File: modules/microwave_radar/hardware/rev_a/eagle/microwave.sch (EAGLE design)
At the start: 55 parts, among them J1 MODULE_GENERIC, J2 TC2030-JLINK-L, U1 SAM4LC8AA, U2 TLV62130, U3 MSGEQ7

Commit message: First try of routing. Fill in several attributes
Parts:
- C10, C11, C12, C14, C9: DIGIKEY (none) -> 490-10777-1-ND
- C13: DIGIKEY (none) -> 490-13252-1-ND
- C6, C8: DIGIKEY (none) -> 490-8230-1-ND
- L1: DIGIKEY (none) -> 490-5216-1-ND
- R10, R9: DIGIKEY (none) -> 1276-3432-1-ND
- R11: DIGIKEY (none) -> 1276-3431-1-ND
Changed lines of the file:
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@@
 </part>
 <part name="X1" library="crystals" deviceset="FH1600015" device=""/>
-<part name="C6" library="passives" deviceset="CAPACITOR" device="0402_CAP" value="8pF"/>
-<part name="C8" library="passives" deviceset="CAPACITOR" device="0402_CAP" value="8pF"/>
+<part name="C6" library="passives" deviceset="CAPACITOR" device="0402_CAP" value="8pF">
+<attribute name="DIGIKEY" value="490-8230-1-ND"/>
+</part>
+<part name="C8" library="passives" deviceset="CAPACITOR" device="0402_CAP" value="8pF">
+<attribute name="DIGIKEY" value="490-8230-1-ND"/>
+</part>
 <part name="SUPPLY5" library="supply1" deviceset="GND" device=""/>
 <part name="SUPPLY6" library="supply1" deviceset="GND" device=""/>
 <part name="J2" library="connector" deviceset="TC2030-JLINK" device="-L"/>
 <part name="SUPPLY7" library="supply1" deviceset="GND" device=""/>
-<part name="R9" library="passives" deviceset="RESISTOR" device="0402_RES" value="100k"/>
-<part name="R10" library="passives" deviceset="RESISTOR" device="0402_RES" value="100k"/>
-<part name="C9" library="passives" deviceset="CAPACITOR" device="0402_CAP" value="100n"/>
-<part name="C10" library="passives" deviceset="CAPACITOR" device="0402_CAP" value="100n"/>
-<part name="C11" library="passives" deviceset="CAPACITOR" device="0402_CAP" value="100n"/>
-<part name="L1" library="passives" deviceset="FERRITE_BEAD" device="0402" value="1.5k"/>
-<part name="C12" library="passives" deviceset="CAPACITOR" device="0402_CAP" value="100n"/>
+<part name="R9" library="passives" deviceset="RESISTOR" device="0402_RES" value="100k">
+<attribute name="DIGIKEY" value="1276-3432-1-ND"/>
+</part>
+<part name="R10" library="passives" deviceset="RESISTOR" device="0402_RES" value="100k">
+<attribute name="DIGIKEY" value="1276-3432-1-ND"/>
+</part>
+<part name="C9" library="passives" deviceset="CAPACITOR" device="0402_CAP" value="100n">
+<attribute name="DIGIKEY" value="490-10777-1-ND"/>
+</part>
+<part name="C10" library="passives" deviceset="CAPACITOR" device="0402_CAP" value="100n">
+<attribute name="DIGIKEY" value="490-10777-1-ND"/>
+</part>
+<part name="C11" library="passives" deviceset="CAPACITOR" device="0402_CAP" value="100n">
+<attribute name="DIGIKEY" value="490-10777-1-ND"/>
+</part>
+<part name="L1" library="passives" deviceset="FERRITE_BEAD" device="0402" value="1.5k">
+<attribute name="DIGIKEY" value="490-5216-1-ND"/>
+</part>
+<part name="C12" library="passives" deviceset="CAPACITOR" device="0402_CAP" value="100n">
+<attribute name="DIGIKEY" value="490-10777-1-ND"/>
+</part>
 <part name="L2" library="signpost" deviceset="LHQ3NP" device="" value="22uH"/>
-<part name="C13" library="passives" deviceset="CAPACITOR" device="0402_CAP" value="100n"/>
-<part name="C14" library="passives" deviceset="CAPACITOR" device="0402_CAP" value="100n"/>
+<part name="C13" library="passives" deviceset="CAPACITOR" device="0402_CAP" value="100n">
+<attribute name="DIGIKEY" value="490-13252-1-ND"/>
+</part>
+<part name="C14" library="passives" deviceset="CAPACITOR" device="0402_CAP" value="100n">
+<attribute name="DIGIKEY" value="490-10777-1-ND"/>
+</part>
 <part name="R1" library="passives" deviceset="RESISTOR" device="0402_RES" value="12k"/>
 <part name="C1" library="passives" deviceset="CAPACITOR" device="0402_CAP" value="4.7u"/>
@@
 <part name="C7" library="passives" deviceset="CAPACITOR" device="0402_CAP" value="2.2n"/>
 <part name="R8" library="passives" deviceset="RESISTOR" device="0402_RES" value="100k"/>
-<part name="R11" library="passives" deviceset="RESISTOR" device="0402_RES" value="10k"/>
+<part name="R11" library="passives" deviceset="RESISTOR" device="0402_RES" value="10k">
+<attribute name="DIGIKEY" value="1276-3431-1-ND"/>
+</part>
 <part name="FRAME4" library="lab11-frames" deviceset="LETTER_L_UMICH" device=""/>
 <part name="U2" library="chips" deviceset="TLV62130" device=""/>
@@
 </instance>
 <instance part="X1" gate="G$1" x="218.44" y="165.1" rot="R90"/>
-<instance part="C6" gate="G$1" x="223.52" y="170.18" rot="R90"/>
-<instance part="C8" gate="G$1" x="223.52" y="160.02" rot="R90"/>
+<instance part="C6" gate="G$1" x="223.52" y="170.18" rot="R90">
+<attribute name="DIGIKEY" x="223.52" y="170.18" size="1.778" layer="96" rot="R90" display="off"/>
+</instance>
+<instance part="C8" gate="G$1" x="223.52" y="160.02" rot="R90">
+<attribute name="DIGIKEY" x="223.52" y="160.02" size="1.778" layer="96" rot="R90" display="off"/>
+</instance>
 <instance part="SUPPLY5" gate="1" x="233.68" y="154.94"/>
 <instance part="SUPPLY6" gate="1" x="50.8" y="60.96"/>
 <instance part="J2" gate="G$1" x="177.8" y="40.64"/>
 <instance part="SUPPLY7" gate="1" x="160.02" y="30.48"/>
-<instance part="R9" gate="G$1" x="195.58" y="55.88" rot="R90"/>
-<instance part="R10" gate="G$1" x="203.2" y="55.88" rot="R90"/>
-<instance part="C9" gate="G$1" x="55.88" y="101.6" rot="R180"/>
-<instance part="C10" gate="G$1" x="63.5" y="101.6" rot="R180"/>
-<instance part="C11" gate="G$1" x="71.12" y="101.6" rot="R180"/>
-<instance part="L1" gate="G$1" x="81.28" y="104.14" rot="R90"/>
-<instance part="C12" gate="G$1" x="81.28" y="86.36" rot="R180"/>
+<instance part="R9" gate="G$1" x="195.58" y="55.88" rot="R90">
+<attribute name="DIGIKEY" x="195.58" y="55.88" size="1.778" layer="96" rot="R90" display="off"/>
+</instance>
+<instance part="R10" gate="G$1" x="203.2" y="55.88" rot="R90">
+<attribute name="DIGIKEY" x="203.2" y="55.88" size="1.778" layer="96" rot="R90" display="off"/>
+</instance>
+<instance part="C9" gate="G$1" x="55.88" y="101.6" rot="R180">
+<attribute name="DIGIKEY" x="55.88" y="101.6" size="1.778" layer="96" rot="R180" display="off"/>
+</instance>
+<instance part="C10" gate="G$1" x="63.5" y="101.6" rot="R180">
+<attribute name="DIGIKEY" x="63.5" y="101.6" size="1.778" layer="96" rot="R180" display="off"/>
+</instance>
+<instance part="C11" gate="G$1" x="71.12" y="101.6" rot="R180">
+<attribute name="DIGIKEY" x="71.12" y="101.6" size="1.778" layer="96" rot="R180" display="off"/>
+</instance>
+<instance part="L1" gate="G$1" x="81.28" y="104.14" rot="R90">
+<attribute name="DIGIKEY" x="81.28" y="104.14" size="1.778" layer="96" rot="R90" display="off"/>
+</instance>
+<instance part="C12" gate="G$1" x="81.28" y="86.36" rot="R180">
+<attribute name="DIGIKEY" x="81.28" y="86.36" size="1.778" layer="96" rot="R180" display="off"/>
+</instance>
 <instance part="L2" gate="G$1" x="93.98" y="88.9" rot="R90"/>
-<instance part="C13" gate="G$1" x="91.44" y="76.2" rot="R180"/>
-<instance part="C14" gate="G$1" x="99.06" y="76.2" rot="R180"/>
-<instance part="R11" gate="G$1" x="187.96" y="129.54"/>
+<instance part="C13" gate="G$1" x="91.44" y="76.2" rot="R180">
+<attribute name="DIGIKEY" x="91.44" y="76.2" size="1.778" layer="96" rot="R180" display="off"/>
+</instance>
+<instance part="C14" gate="G$1" x="99.06" y="76.2" rot="R180">
+<attribute name="DIGIKEY" x="99.06" y="76.2" size="1.778" layer="96" rot="R180" display="off"/>
+</instance>
+<instance part="R11" gate="G$1" x="187.96" y="129.54">
+<attribute name="DIGIKEY" x="187.96" y="129.54" size="1.778" layer="96" display="off"/>
+</instance>
 <instance part="J1" gate="G$1" x="22.86" y="142.24"/>
 <instance part="+3V4" gate="G$1" x="50.8" y="127"/>

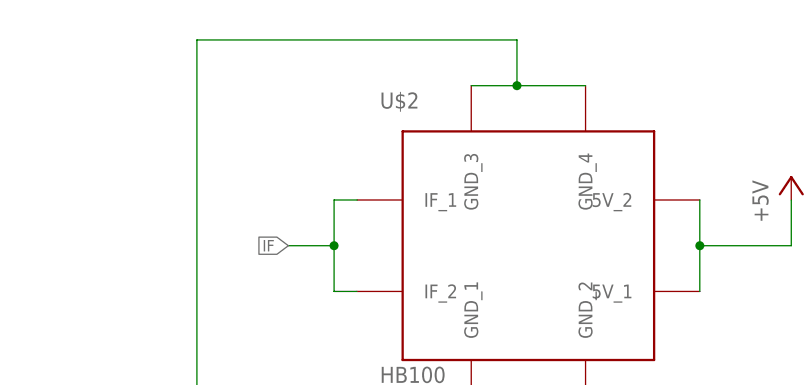
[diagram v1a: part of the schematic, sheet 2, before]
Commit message: Finish routing. Fix library dollar sign bug
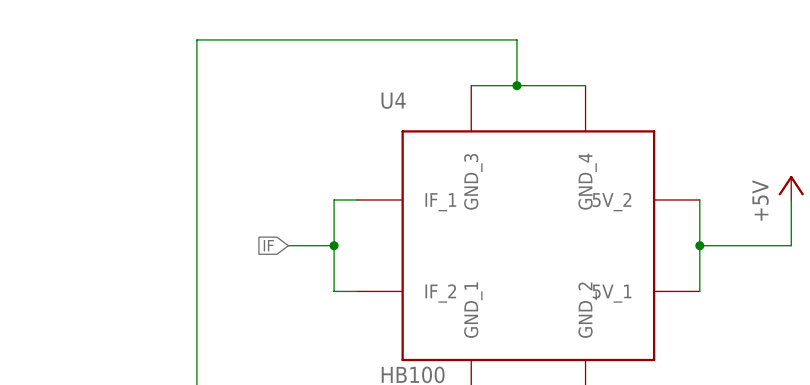
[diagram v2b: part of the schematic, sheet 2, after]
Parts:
- removed U$2: HB100, microwave_radar:HB100
- added U4: HB100, microwave_radar:HB100
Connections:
- net +5V: now also U4.5V_1, U4.5V_2; no longer U$2.5V_1, U$2.5V_2
- net GND: now also U4.GND_1, U4.GND_2, U4.GND_3, U4.GND_4; no longer U$2.GND_1, U$2.GND_2, U$2.GND_3, U$2.GND_4
- net IF: now also U4.IF_1, U4.IF_2; no longer U$2.IF_1, U$2.IF_2
- net N$2: now also C22.2
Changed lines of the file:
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@@
 <part name="TP1" library="headers" deviceset="TEST_POINT_0.040IN" device=""/>
 <part name="TP2" library="headers" deviceset="TEST_POINT_0.040IN" device=""/>
-<part name="U$2" library="microwave_radar" deviceset="HB100" device=""/>
 <part name="GND6" library="umich" deviceset="GND" device=""/>
 <part name="J1" library="signpost" deviceset="MODULE_GENERIC" device=""/>
@@
 <part name="GND7" library="umich" deviceset="GND" device=""/>
 <part name="TP6" library="headers" deviceset="TEST_POINT_0.040IN" device=""/>
+<part name="U4" library="microwave_radar" deviceset="HB100" device=""/>
 </parts>
 <sheets>
@@
 <instance part="C7" gate="G$1" x="127" y="25.4" rot="R90"/>
 <instance part="R8" gate="G$1" x="127" y="12.7" rot="R180"/>
-<instance part="U$2" gate="G$1" x="160.02" y="116.84"/>
 <instance part="GND6" gate="1" x="157.48" y="88.9"/>
 <instance part="+3V1" gate="G$1" x="22.86" y="109.22"/>
@@
 <instance part="+3V3" gate="G$1" x="76.2" y="139.7"/>
 <instance part="GND7" gate="1" x="76.2" y="104.14"/>
+<instance part="U4" gate="G1" x="160.02" y="116.84"/>
 </instances>
 <busses>
@@
 </segment>
 <segment>
-<pinref part="U$2" gate="G$1" pin="GND_1"/>
 <wire x1="152.4" y1="99.06" x2="152.4" y2="96.52" width="0.1524" layer="91"/>
 <wire x1="152.4" y1="96.52" x2="157.48" y2="96.52" width="0.1524" layer="91"/>
 <wire x1="157.48" y1="96.52" x2="165.1" y2="96.52" width="0.1524" layer="91"/>
 <wire x1="165.1" y1="96.52" x2="165.1" y2="99.06" width="0.1524" layer="91"/>
-<pinref part="U$2" gate="G$1" pin="GND_2"/>
 <pinref part="GND6" gate="1" pin="GND"/>
 <wire x1="157.48" y1="91.44" x2="157.48" y2="96.52" width="0.1524" layer="91"/>
 <junction x="157.48" y="96.52"/>
-<pinref part="U$2" gate="G$1" pin="GND_4"/>
 <wire x1="165.1" y1="134.62" x2="157.48" y2="134.62" width="0.1524" layer="91"/>
-<pinref part="U$2" gate="G$1" pin="GND_3"/>
 <wire x1="157.48" y1="134.62" x2="152.4" y2="134.62" width="0.1524" layer="91"/>
 <wire x1="157.48" y1="134.62" x2="157.48" y2="139.7" width="0.1524" layer="91"/>
@@
 <wire x1="121.92" y1="96.52" x2="152.4" y2="96.52" width="0.1524" layer="91"/>
 <junction x="152.4" y="96.52"/>
+<pinref part="U4" gate="G1" pin="GND_1"/>
+<pinref part="U4" gate="G1" pin="GND_2"/>
+<pinref part="U4" gate="G1" pin="GND_3"/>
+<pinref part="U4" gate="G1" pin="GND_4"/>
 </segment>
 <segment>
@@
 <net name="+5V" class="0">
 <segment>
-<pinref part="U$2" gate="G$1" pin="5V_2"/>
 <wire x1="177.8" y1="121.92" x2="177.8" y2="116.84" width="0.1524" layer="91"/>
-<pinref part="U$2" gate="G$1" pin="5V_1"/>
 <wire x1="177.8" y1="116.84" x2="177.8" y2="111.76" width="0.1524" layer="91"/>
 <wire x1="177.8" y1="116.84" x2="187.96" y2="116.84" width="0.1524" layer="91"/>
@@
 <pinref part="P+2" gate="1" pin="+5V"/>
 <wire x1="187.96" y1="116.84" x2="187.96" y2="121.92" width="0.1524" layer="91"/>
+<pinref part="U4" gate="G1" pin="5V_1"/>
+<pinref part="U4" gate="G1" pin="5V_2"/>
 </segment>
 </net>
 <net name="IF" class="0">
 <segment>
-<pinref part="U$2" gate="G$1" pin="IF_1"/>
 <wire x1="139.7" y1="121.92" x2="137.16" y2="121.92" width="0.1524" layer="91"/>
 <wire x1="137.16" y1="121.92" x2="137.16" y2="116.84" width="0.1524" layer="91"/>
 <wire x1="137.16" y1="116.84" x2="137.16" y2="111.76" width="0.1524" layer="91"/>
 <wire x1="137.16" y1="111.76" x2="139.7" y2="111.76" width="0.1524" layer="91"/>
-<pinref part="U$2" gate="G$1" pin="IF_2"/>
 <wire x1="137.16" y1="116.84" x2="132.08" y2="116.84" width="0.1524" layer="91"/>
 <junction x="137.16" y="116.84"/>
 <label x="132.08" y="116.84" size="1.27" layer="95" font="vector" rot="R180" xref="yes"/>
+<pinref part="U4" gate="G1" pin="IF_1"/>
+<pinref part="U4" gate="G1" pin="IF_2"/>
 </segment>
 <segment>
@@
 <segment>
 <pinref part="R15" gate="G$1" pin="1"/>
-<wire x1="132.08" y1="50.8" x2="132.08" y2="58.42" width="0.1524" layer="91"/>
+<wire x1="132.08" y1="53.34" x2="132.08" y2="58.42" width="0.1524" layer="91"/>
 <pinref part="U3" gate="G$1" pin="CLK"/>
 <wire x1="111.76" y1="58.42" x2="132.08" y2="58.42" width="0.1524" layer="91"/>
 <junction x="132.08" y="58.42"/>
-</segment>
-</net>
+<pinref part="C22" gate="G$1" pin="2"/>
+</segment>
+</net>
